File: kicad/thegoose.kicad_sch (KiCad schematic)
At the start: 0 parts

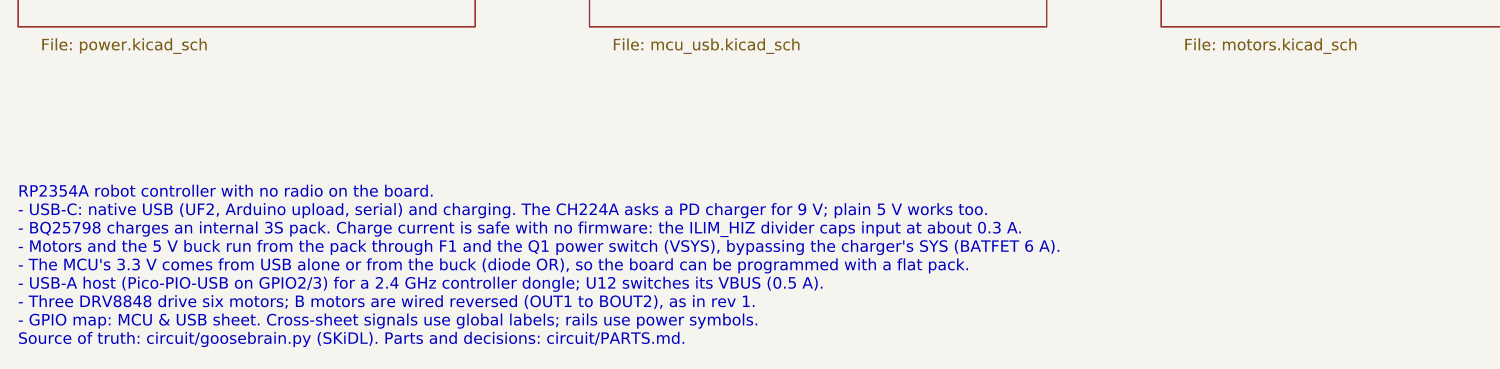
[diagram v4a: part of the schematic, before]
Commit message: Fix the buck inductor, soft-start VSYS and limit motor current
Circuit (goosebrain.py, PARTS.md, schematic):
- L1 is a Coilcraft XAL5030-222 (Isat 9.2 A, the AP64500's max current
  limit). The old CR4030 saturated at about 3.1 A.
- VSYS soft start and clamp: C71 gate-drain and C72 gate-source on Q1,
  R40 27k, R41 10k, and an SMF14A TVS (D4) on VSYS.
- Each DRV8848 chops at about 1.33 A per bridge: 0.15 R sense resistors
  on AISEN/BISEN and a 15k/10k VREF divider from VINT, so six stalled
  motors can't reach the protector's OCD1 trip.
- U4 gets a second 10 uF (C73) and a 100 nF (C74) at VIN.
- Stock swaps after a full JLC stock check: D4 to the Littelfuse SMF14A,
  the sense resistors to YAGEO RL1206FR-7W0R15L (500 mW).

Board:
- New parts placed and routed. The sense resistors are close to their
  pins; U2's B-side runs on F.Cu only.
- 22 more VSYS vias (Q1 drain to the In3 plane, each driver's VM caps,
  both ends of U4's VIN jumper).
- C63 (AVDD) and C68 (SRP-SRN) moved next to the BQ7791501.
- Goose logo on the back silkscreen.
- Review 63: DRC 0 errors, unrouted 0, parity clean, no new DRC types.

tools/fab.py adds per-package rotation offsets read off JLC's placement
preview. The README covers them, the D4 polarity check, the corrected
current limits and the low-stock parts.

Co-Authored-By: Claude Opus 5.5 <noreply@anthropic.com>
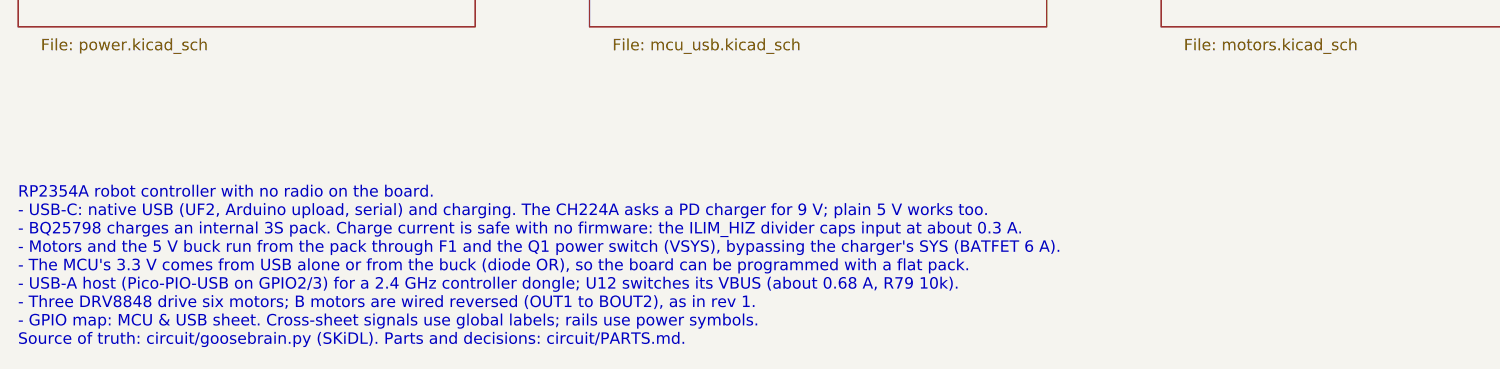
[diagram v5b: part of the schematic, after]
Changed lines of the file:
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@@
 		)
 	)
-	(text "RP2354A robot controller with no radio on the board.\n- USB-C: native USB (UF2, Arduino upload, serial) and charging. The CH224A asks a PD charger for 9 V; plain 5 V works too.\n- BQ25798 charges an internal 3S pack. Charge current is safe with no firmware: the ILIM_HIZ divider caps input at about 0.3 A.\n- Motors and the 5 V buck run from the pack through F1 and the Q1 power switch (VSYS), bypassing the charger's SYS (BATFET 6 A).\n- The MCU's 3.3 V comes from USB alone or from the buck (diode OR), so the board can be programmed with a flat pack.\n- USB-A host (Pico-PIO-USB on GPIO2/3) for a 2.4 GHz controller dongle; U12 switches its VBUS (0.5 A).\n- Three DRV8848 drive six motors; B motors are wired reversed (OUT1 to BOUT2), as in rev 1.\n- GPIO map: MCU & USB sheet. Cross-sheet signals use global labels; rails use power symbols.\nSource of truth: circuit/goosebrain.py (SKiDL). Parts and decisions: circuit/PARTS.md."
+	(text "RP2354A robot controller with no radio on the board.\n- USB-C: native USB (UF2, Arduino upload, serial) and charging. The CH224A asks a PD charger for 9 V; plain 5 V works too.\n- BQ25798 charges an internal 3S pack. Charge current is safe with no firmware: the ILIM_HIZ divider caps input at about 0.3 A.\n- Motors and the 5 V buck run from the pack through F1 and the Q1 power switch (VSYS), bypassing the charger's SYS (BATFET 6 A).\n- The MCU's 3.3 V comes from USB alone or from the buck (diode OR), so the board can be programmed with a flat pack.\n- USB-A host (Pico-PIO-USB on GPIO2/3) for a 2.4 GHz controller dongle; U12 switches its VBUS (about 0.68 A, R79 10k).\n- Three DRV8848 drive six motors; B motors are wired reversed (OUT1 to BOUT2), as in rev 1.\n- GPIO map: MCU & USB sheet. Cross-sheet signals use global labels; rails use power symbols.\nSource of truth: circuit/goosebrain.py (SKiDL). Parts and decisions: circuit/PARTS.md."
 		(exclude_from_sim no)
 		(at 25.4 81.28 0)

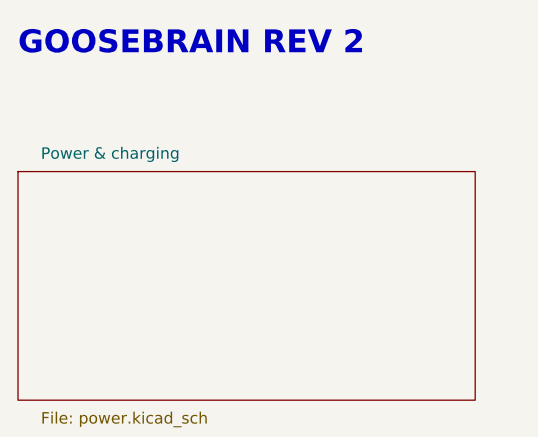
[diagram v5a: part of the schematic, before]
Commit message: Split into brain + smart pack, and support 2S packs
Brain/pack split: charging, protection and the fuse move off the brain
into a separate smart pack board (kicad-pack/goosepack), with its own
USB-C charging port. The brain drops to 4 layers, loses the charger,
PD sink, protector and SY6280, and swaps the DRV8848s for DRV8871s.

2S support on the brain:
- DRV8871 -> DRV8251A (same HSOP-8 footprint, 4.5-48 V VM). Shared VREF
  divider R107/R108/C81 from +3V3 (2.53 V) and 1.18k IPROPI resistors
  keep the 1.36 A limit.
- Q1 gate divider 27k/10k -> 47k/4.7k for -5.1 V drive at an empty 2S
  pack; C71 4.7n -> 10n to keep the ~70 us soft start.

New 2S pack variant (kicad-pack-2s/goosepack2s): BQ25798 PROG 8.2k
(2S, 750 kHz), ILIM R33 18k (~0.42 A charge), ABLIC S-8252AAH protector
in place of the BQ7791501, two HY2213-BB3A balancers with AO3400A and
47R 2512 bleed resistors, 3-pin XH balance header, R94 4.7k for trip
recovery. fab.py builds it with --board pack2s.

Several new parts still need LCSC numbers; fab.py flags each one.

Co-Authored-By: Claude Opus 5.5 <noreply@anthropic.com>
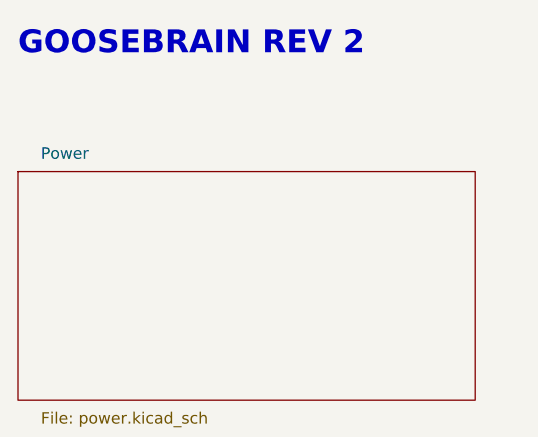
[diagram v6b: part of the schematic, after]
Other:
- sheet Power & charging renamed Power
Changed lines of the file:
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@@
     (stroke (width 0.0006) (type default))
     (fill (color 0 0 0 0.0000))
-    (property "Sheetname" "Power & charging" (at 27.94 36.83 0)
+    (property "Sheetname" "Power" (at 27.94 36.83 0)
       (effects (font (size 1.27 1.27)) (justify left bottom))
     )

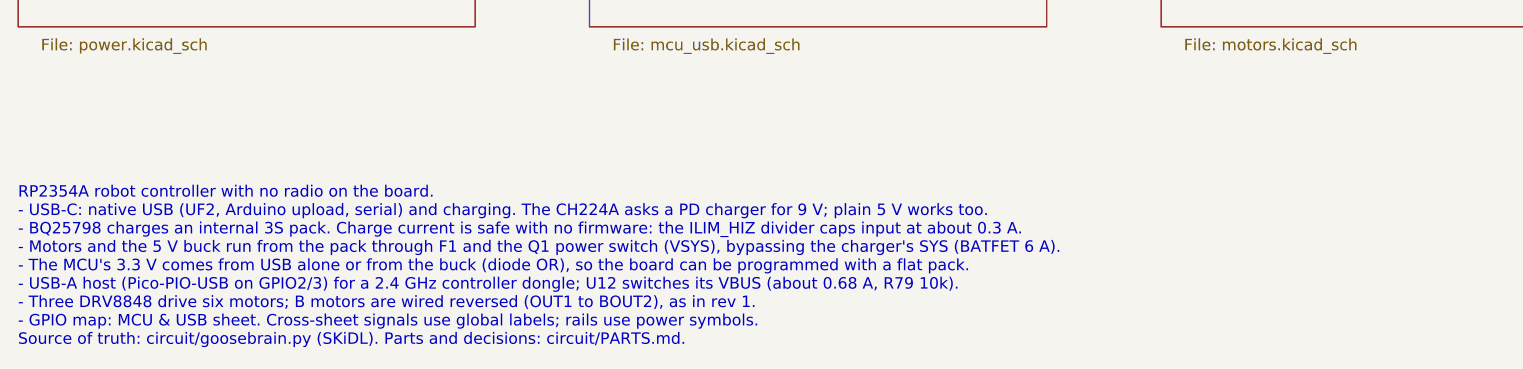
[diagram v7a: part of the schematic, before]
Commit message: Place the brain double-sided at 66.3 x 34 mm, unrouted
- tools/place_double.py rebuilds the placement from scratch: parts on both
  sides, M1-M6 swapped to JST PH S2B-PH-K (C173752), J3 under J4, the
  switches in the bottom-right corner, the USB-C ESD and series resistors
  on the front between J1 and U10.
- Pulls in the 2026-10-20 schematic change (IO5/IO6 off the ADC pins,
  R109/R114 15k USB-A pull-downs).
- Reassigns U10 GPIOs for the new layout, keeping each motor on its own
  PWM slice and IO4-IO6 on slices 1 and 4; USB-A moves to GPIO26/27.
- Adds back-side fiducials FID4-FID6.
- The old partial autoroute is kept in kicad/reference/.

Co-Authored-By: Claude Opus 5.5 <noreply@anthropic.com>
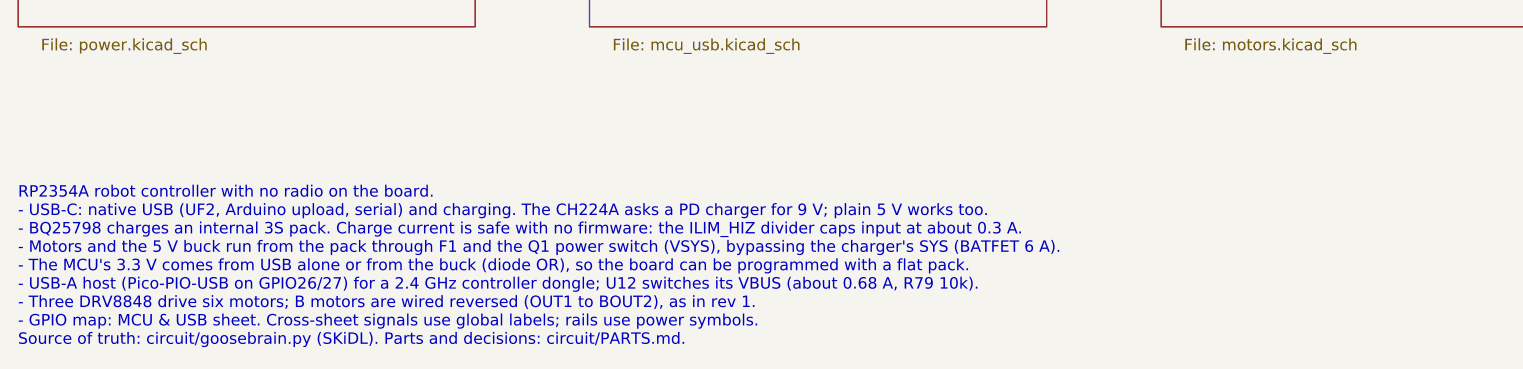
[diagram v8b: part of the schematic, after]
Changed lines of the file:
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@@
 		)
 	)
-	(text "RP2354A robot controller with no radio on the board.\n- USB-C: native USB (UF2, Arduino upload, serial) and charging. The CH224A asks a PD charger for 9 V; plain 5 V works too.\n- BQ25798 charges an internal 3S pack. Charge current is safe with no firmware: the ILIM_HIZ divider caps input at about 0.3 A.\n- Motors and the 5 V buck run from the pack through F1 and the Q1 power switch (VSYS), bypassing the charger's SYS (BATFET 6 A).\n- The MCU's 3.3 V comes from USB alone or from the buck (diode OR), so the board can be programmed with a flat pack.\n- USB-A host (Pico-PIO-USB on GPIO2/3) for a 2.4 GHz controller dongle; U12 switches its VBUS (about 0.68 A, R79 10k).\n- Three DRV8848 drive six motors; B motors are wired reversed (OUT1 to BOUT2), as in rev 1.\n- GPIO map: MCU & USB sheet. Cross-sheet signals use global labels; rails use power symbols.\nSource of truth: circuit/goosebrain.py (SKiDL). Parts and decisions: circuit/PARTS.md."
+	(text "RP2354A robot controller with no radio on the board.\n- USB-C: native USB (UF2, Arduino upload, serial) and charging. The CH224A asks a PD charger for 9 V; plain 5 V works too.\n- BQ25798 charges an internal 3S pack. Charge current is safe with no firmware: the ILIM_HIZ divider caps input at about 0.3 A.\n- Motors and the 5 V buck run from the pack through F1 and the Q1 power switch (VSYS), bypassing the charger's SYS (BATFET 6 A).\n- The MCU's 3.3 V comes from USB alone or from the buck (diode OR), so the board can be programmed with a flat pack.\n- USB-A host (Pico-PIO-USB on GPIO26/27) for a 2.4 GHz controller dongle; U12 switches its VBUS (about 0.68 A, R79 10k).\n- Three DRV8848 drive six motors; B motors are wired reversed (OUT1 to BOUT2), as in rev 1.\n- GPIO map: MCU & USB sheet. Cross-sheet signals use global labels; rails use power symbols.\nSource of truth: circuit/goosebrain.py (SKiDL). Parts and decisions: circuit/PARTS.md."
 		(exclude_from_sim no)
 		(at 25.4 81.28 0)
